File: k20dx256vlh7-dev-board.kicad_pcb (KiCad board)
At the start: 2 copper layers, 41 parts, among them J1 Conn_01x21_Male, J2 Conn_01x21_Male, J3 Conn_01x21_Male, J4 Conn_01x21_Male, J5 USB_C_Receptacle_USB2.0, J6 Conn_01x06_Male, SW1 Program, SW2 Reset, U1 MCP2562-E-SN, U2 MK20DX256VLH7, U3 NJM2884U1, U4 MKL04Z32VLC4, Y1 16MHz

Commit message: 回路図を更新
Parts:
- removed C3: 0.1u, Capacitor_SMD:C_0603_1608Metric
- removed C8: 2.2u, Capacitor_SMD:C_0805_2012Metric
- J1, J2, J3, J4, J6: moved to B.Cu
- moved SW2 116.0 mm to (223.5, 80.0), turned to 90 degrees
- moved J3 113.1 mm to (228.6, 127.0)
- moved J1 106.7 mm to (226.1, 127.0)
- moved J2 101.2 mm to (205.7, 127.0)
- moved J4 99.4 mm to (208.3, 127.0)
- moved C1 93.9 mm to (217.2, 116.6)
- moved R9 90.0 mm to (223.5, 86.9), turned to 270 degrees
- moved C9 86.7 mm to (223.5, 107.4), turned to 270 degrees
- moved J6 86.3 mm to (223.5, 76.2), turned to 90 degrees
- moved C4 85.2 mm to (222.0, 108.9), turned to 270 degrees
- moved R8 83.7 mm to (223.4, 123.6), turned to 90 degrees
- moved R1 81.8 mm to (220.9, 118.7), turned to 180 degrees
- moved C10 81.7 mm to (217.0, 118.4), turned to 180 degrees
- moved Y1 81.1 mm to (223.5, 91.4), turned to 90 degrees
- moved D2 78.3 mm to (220.0, 109.4)
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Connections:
- J1 pad 1: +5V -> GND
- J1 pad 15: Net-(J1-Pad15) -> /INTERNAL_LED
- J1 pad 16: /INTERNAL_LED -> Net-(J1-Pad16)
- J1 pad 2: +3V3 -> Net-(J1-Pad2)
- J1 pad 5: Net-(J1-Pad5) -> /CAN+
- J1 pad 6: /CAN+ -> /CAN-
- J1 pad 7: /CAN- -> Net-(J1-Pad7)
- J2 pad 1: GND -> +5V
- J2 pad 2: Net-(J2-Pad2) -> +3V3
- J3 pad 1: +5V -> GND
- J3 pad 15: Net-(J1-Pad15) -> /INTERNAL_LED
- J3 pad 16: /INTERNAL_LED -> Net-(J1-Pad16)
- J3 pad 2: +3V3 -> Net-(J1-Pad2)
- J3 pad 5: Net-(J1-Pad5) -> /CAN+
- J3 pad 6: /CAN+ -> /CAN-
- J3 pad 7: /CAN- -> Net-(J1-Pad7)
- J4 pad 1: GND -> +5V
- J4 pad 2: Net-(J2-Pad2) -> +3V3
- U2 pad 1: Net-(J2-Pad9) -> Net-(J2-Pad10)
- U2 pad 10: Net-(J2-Pad6) -> Net-(J2-Pad7)
- U2 pad 11: Net-(J2-Pad4) -> Net-(J2-Pad5)
- U2 pad 12: Net-(J2-Pad3) -> Net-(J2-Pad4)
- U2 pad 18: Net-(J2-Pad2) -> Net-(J2-Pad3)
- U2 pad 2: Net-(J2-Pad14) -> Net-(J2-Pad15)
- U2 pad 26: Net-(J2-Pad7) -> Net-(J2-Pad8)
- U2 pad 27: Net-(J2-Pad16) -> Net-(J2-Pad17)
- U2 pad 35: Net-(J1-Pad19) -> Net-(J1-Pad18)
- U2 pad 36: Net-(J1-Pad20) -> Net-(J1-Pad19)
- U2 pad 37: Net-(J2-Pad21) -> Net-(J1-Pad21)
- U2 pad 38: Net-(J1-Pad21) -> Net-(J1-Pad20)
- U2 pad 39: Net-(J1-Pad3) -> Net-(J1-Pad2)
- U2 pad 40: Net-(J1-Pad4) -> Net-(J1-Pad3)
- U2 pad 41: Net-(J2-Pad8) -> Net-(J2-Pad9)
- U2 pad 42: Net-(J2-Pad15) -> Net-(J2-Pad16)
- U2 pad 43: Net-(J1-Pad18) -> Net-(J1-Pad17)
- U2 pad 44: Net-(J2-Pad18) -> Net-(J2-Pad19)
- U2 pad 45: Net-(J2-Pad17) -> Net-(J2-Pad18)
- U2 pad 46: Net-(J1-Pad12) -> Net-(J1-Pad11)
- U2 pad 49: Net-(J1-Pad13) -> Net-(J1-Pad12)
- U2 pad 51: Net-(J1-Pad14) -> Net-(J1-Pad13)
- U2 pad 52: Net-(J1-Pad15) -> Net-(J1-Pad14)
- U2 pad 53: Net-(J2-Pad12) -> Net-(J2-Pad13)
- U2 pad 54: Net-(J2-Pad13) -> Net-(J2-Pad14)
- U2 pad 55: Net-(J2-Pad11) -> Net-(J2-Pad12)
- U2 pad 56: Net-(J2-Pad10) -> Net-(J2-Pad11)
- U2 pad 57: Net-(J1-Pad5) -> Net-(J1-Pad4)
- U2 pad 58: Net-(J1-Pad17) -> Net-(J1-Pad16)
- U2 pad 59: Net-(J1-Pad10) -> Net-(J1-Pad9)
- U2 pad 60: Net-(J1-Pad11) -> Net-(J1-Pad10)
- U2 pad 61: Net-(J1-Pad9) -> Net-(J1-Pad8)
- U2 pad 62: Net-(J2-Pad20) -> Net-(J2-Pad21)
- U2 pad 63: Net-(J2-Pad19) -> Net-(J2-Pad20)
- U2 pad 64: Net-(J1-Pad8) -> Net-(J1-Pad7)
- U2 pad 9: Net-(J2-Pad5) -> Net-(J2-Pad6)
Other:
- board outline added: 25.4 x 53.3 mm
- net class 0.2 added: clearance 0.1778, trace_width 0.2, via_dia 0.8, via_drill 0.4
- net class 0.25 added: clearance 0.1778, trace_width 0.25, via_dia 0.8, via_drill 0.4
- net class 0.5 added: clearance 0.1778, trace_width 0.5, via_dia 0.8, via_drill 0.4

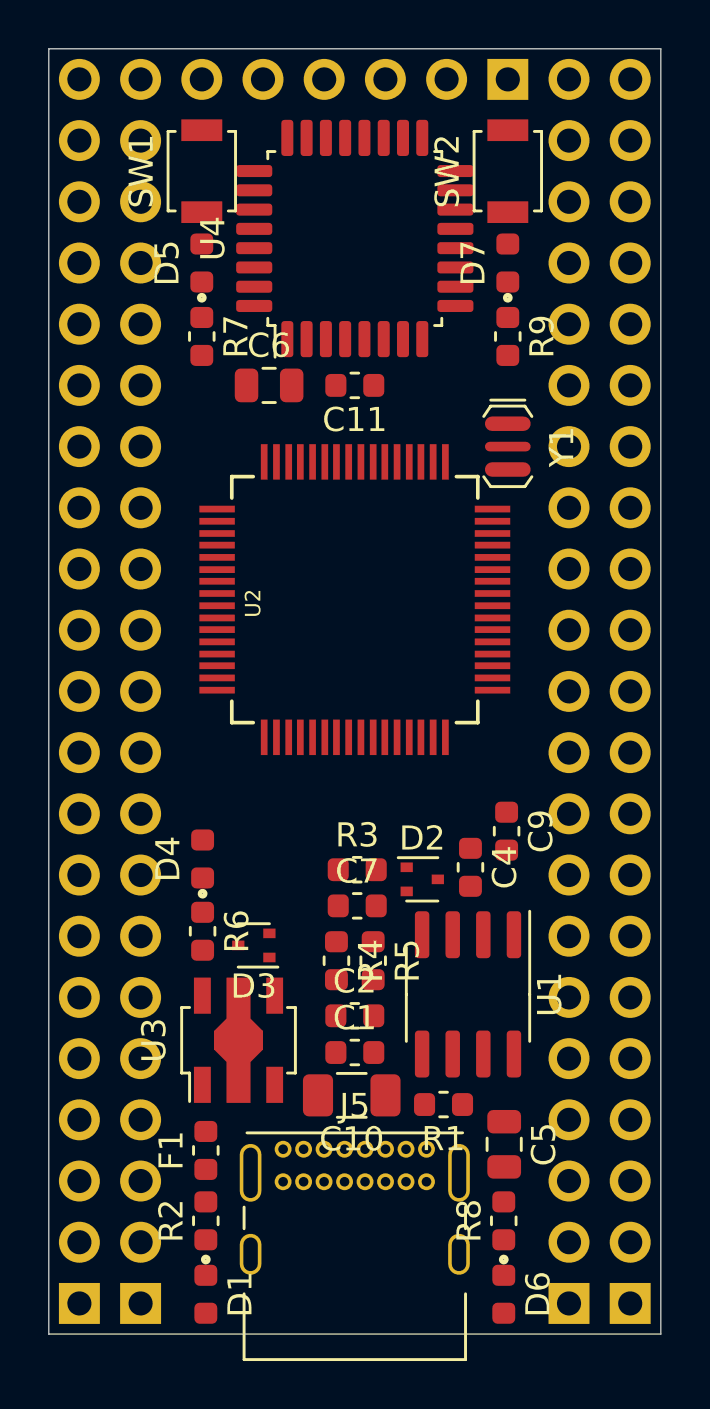
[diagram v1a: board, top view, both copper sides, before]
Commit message: フットプリントの変更
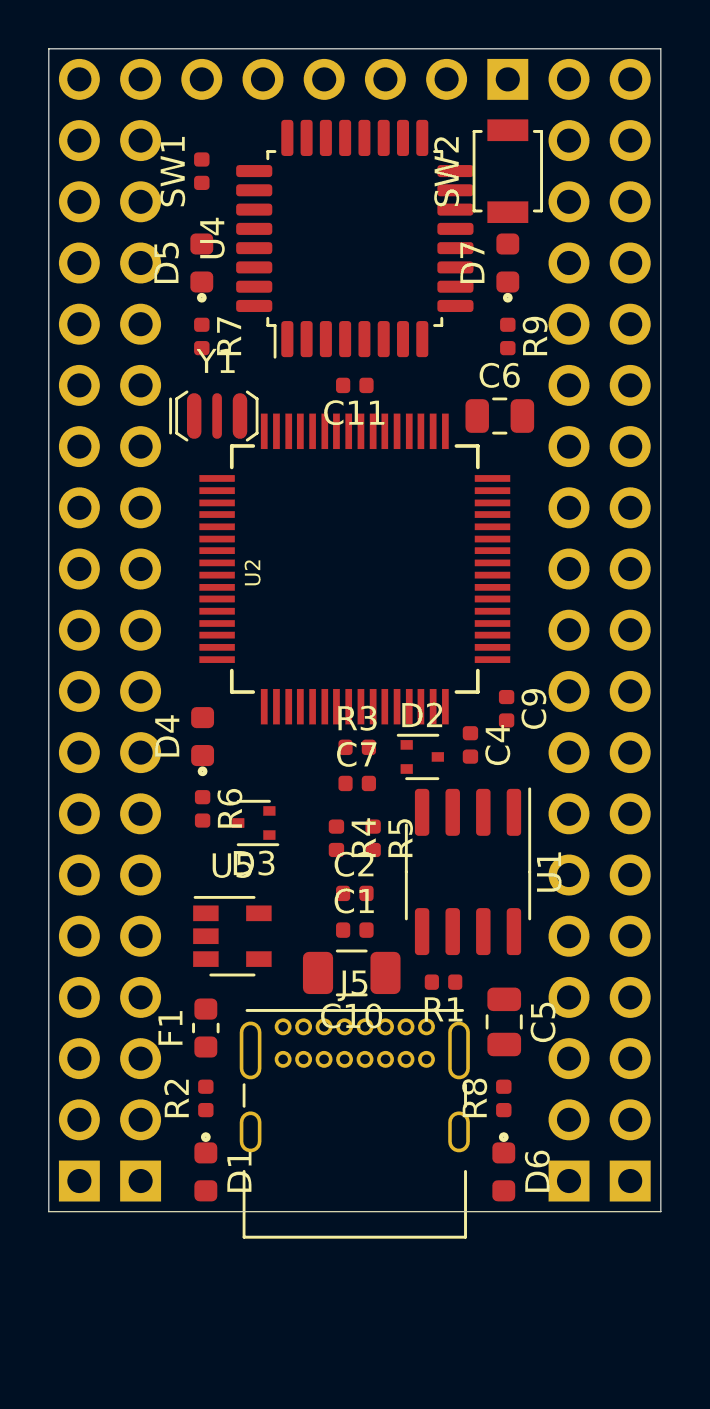
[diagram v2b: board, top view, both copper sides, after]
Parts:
- removed U3: NJM2884U1, Package_TO_SOT_SMD:SOT-89-5
- added U5: MIC5219-3.3YM5, Package_TO_SOT_SMD:SOT-23-5, F.Cu at (212.1, 111.8)
- C1, C11, C2, C4, C7, C9: value 0.1u -> 0.1u, 50v; footprint Capacitor_SMD:C_0603_1608Metric -> Capacitor_SMD:C_0402_1005Metric
- J1, J2, J3, J4: value Conn_01x21_Male -> Conn_01x19_Male; footprint Connector_PinHeader_2.54mm:PinHeader_1x21_P2.54mm_Vertical -> Connector_PinHeader_2.54mm:PinHeader_1x19_P2.54mm_Vertical
- R1, R2, R3, R4, R5, R6, R7, R8, R9: footprint Resistor_SMD:R_0603_1608Metric -> Resistor_SMD:R_0402_1005Metric
- SW1: footprint Button_Switch_SMD:SW_SPST_B3U-1000P -> Capacitor_SMD:C_0402_1005Metric
- moved Y1 12.1 mm to (211.5, 90.2), turned to 180 degrees
- moved C6 9.66 mm to (223.2, 90.2)
- moved J1 5.68 mm to (228.6, 121.9)
- moved J3 5.68 mm to (226.1, 121.9)
- moved C4 5.08 mm to (222.0, 103.8)
- moved C9 5.08 mm to (223.5, 102.3)
- moved D2 5.08 mm to (220.0, 104.3)
- moved F1 5.08 mm to (211.0, 115.6)
- moved C1 5.08 mm to (217.2, 111.5)
- moved C10 5.08 mm to (217.0, 113.3)
- moved C2 5.08 mm to (217.2, 110.0)
- moved C5 5.08 mm to (223.4, 115.3)
- moved C7 5.08 mm to (217.3, 105.4)
- moved D1 5.08 mm to (211.0, 121.5)
- moved D3 5.08 mm to (213.0, 107.1)
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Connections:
- U2 pad 1: Net-(J2-Pad10) -> Net-(J2-Pad6)
- U2 pad 10: Net-(J2-Pad7) -> Net-(U2-Pad10)
- U2 pad 11: Net-(J2-Pad5) -> Net-(U2-Pad11)
- U2 pad 12: Net-(J2-Pad4) -> Net-(U2-Pad12)
- U2 pad 2: Net-(J2-Pad15) -> Net-(J2-Pad11)
- U2 pad 26: Net-(J2-Pad8) -> Net-(J2-Pad4)
- U2 pad 27: Net-(J2-Pad17) -> Net-(J2-Pad13)
- U2 pad 37: Net-(J1-Pad21) -> Net-(J2-Pad18)
- U2 pad 38: Net-(J1-Pad20) -> Net-(J2-Pad19)
- U2 pad 41: Net-(J2-Pad9) -> Net-(J2-Pad5)
- U2 pad 42: Net-(J2-Pad16) -> Net-(J2-Pad12)
- U2 pad 44: Net-(J2-Pad19) -> Net-(J2-Pad15)
- U2 pad 45: Net-(J2-Pad18) -> Net-(J2-Pad14)
- U2 pad 53: Net-(J2-Pad13) -> Net-(J2-Pad9)
- U2 pad 54: Net-(J2-Pad14) -> Net-(J2-Pad10)
- U2 pad 55: Net-(J2-Pad12) -> Net-(J2-Pad8)
- U2 pad 56: Net-(J2-Pad11) -> Net-(J2-Pad7)
- U2 pad 62: Net-(J2-Pad21) -> Net-(J2-Pad17)
- U2 pad 63: Net-(J2-Pad20) -> Net-(J2-Pad16)
- U2 pad 9: Net-(J2-Pad6) -> Net-(U2-Pad9)
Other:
- board size 25.4 x 53.3 mm -> 25.4 x 48.3 mm

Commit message: 回路図の見直し
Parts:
- removed J4: Conn_01x19_Male, Connector_PinHeader_2.54mm:PinHeader_1x19_P2.54mm_Vertical
- removed J6: Conn_01x06_Male, Connector_PinHeader_2.54mm:PinHeader_1x06_P2.54mm_Vertical
- J3: value Conn_01x19_Male -> Conn_01x08_Male; footprint Connector_PinHeader_2.54mm:PinHeader_1x19_P2.54mm_Vertical -> Connector_PinHeader_2.54mm:PinHeader_1x08_P2.54mm_Vertical
- SW1: footprint Capacitor_SMD:C_0402_1005Metric -> Button_Switch_SMD:SW_SPST_B3U-1000P
- moved J3 45.7 mm to (226.1, 76.2), turned to 90 degrees
- moved D3 13.6 mm to (208.5, 119.9), turned to 270 degrees
- moved Y1 12.0 mm to (223.4, 90.3), turned to 135 degrees
- moved R6 9.57 mm to (208.9, 97.1)
- moved D4 9.33 mm to (208.9, 94.3)
- moved D2 8.98 mm to (225.9, 97.6), turned to 270 degrees
- moved C10 8.52 mm to (209.6, 117.3), turned to 0 degrees
- moved R1 7.04 mm to (226.3, 109.2), turned to 270 degrees
- moved C1 6.73 mm to (223.8, 112.8)
- moved R9 6.30 mm to (222.9, 80.6)
- moved R7 6.30 mm to (211.4, 80.6)
- moved F1 6.12 mm to (216.7, 113.3), turned to 0 degrees
- moved C4 5.54 mm to (224.4, 98.8)
- moved D7 5.39 mm to (222.2, 78.6), turned to 180 degrees
- moved D5 5.39 mm to (212.2, 78.6), turned to 0 degrees
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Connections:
- J3 pad 1: GND -> /RESET
- J3 pad 2: Net-(J1-Pad2) -> /PTA0
- J3 pad 3: Net-(J1-Pad3) -> /PTA1
- J3 pad 4: Net-(J1-Pad4) -> /PTA2
- J3 pad 5: /CAN+ -> /PTA3
- J3 pad 6: /CAN- -> /Program
- J3 pad 7: Net-(J1-Pad7) -> +3V3
- J3 pad 8: Net-(J1-Pad8) -> GND
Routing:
- net +3V3: track 0.00 -> 38.1 mm, vias 0 -> 1
- net GND: track 0.00 -> 32.9 mm
- net +5V: track 0.00 -> 25.3 mm
- net /USB_D+: track 0.00 -> 13.0 mm, vias 0 -> 1
- net /USB_D-: track 0.00 -> 13.0 mm, vias 0 -> 1
- net Net-(C5-Pad1): track 0.00 -> 12.1 mm
- net /CAN+: track 0.00 -> 11.4 mm
- net /CAN-: track 0.00 -> 4.65 mm
- net Net-(C4-Pad1): track 0.00 -> 3.09 mm
- net Net-(D1-Pad1): track 0.00 -> 2.95 mm
- net Net-(U2-Pad32): track 0.00 -> 2.32 mm
- net Net-(U2-Pad33): track 0.00 -> 2.32 mm
- net /USB_P: track 0.00 -> 1.65 mm
- net /USB_M: track 0.00 -> 1.65 mm

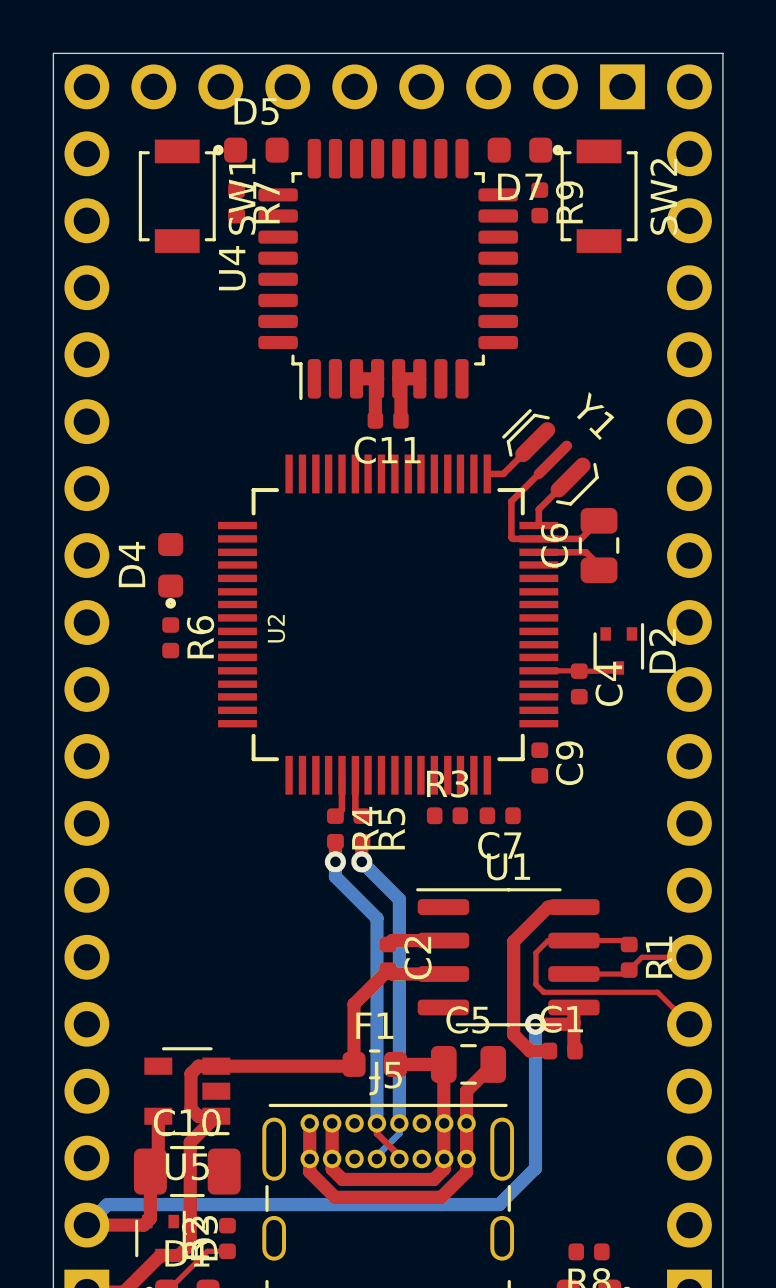
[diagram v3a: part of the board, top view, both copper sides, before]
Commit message: 回路図に追記
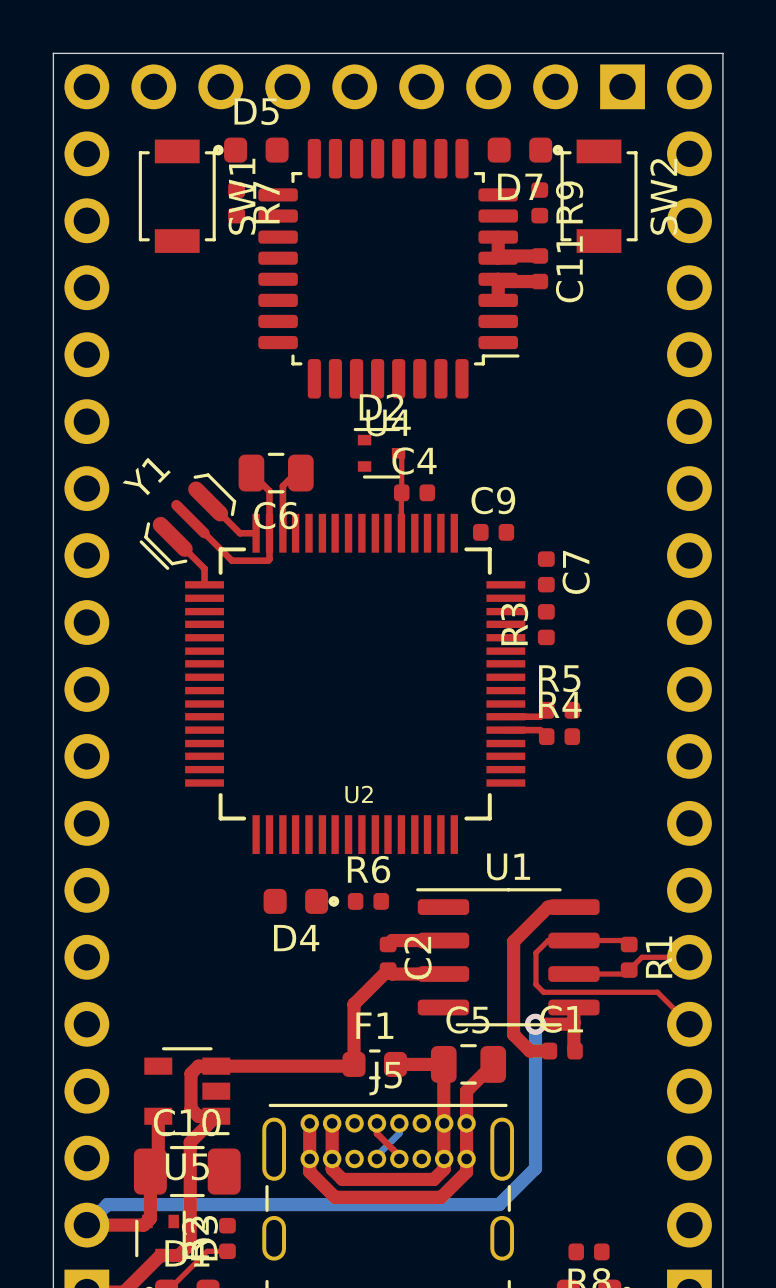
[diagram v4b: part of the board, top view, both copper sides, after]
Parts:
- moved Y1 13.9 mm to (209.7, 92.6), turned to 225 degrees
- moved D4 13.6 mm to (213.7, 107.1), turned to 180 degrees
- moved C6 12.6 mm to (212.9, 90.8), turned to 180 degrees
- moved R6 12.5 mm to (216.4, 107.1), turned to 0 degrees
- moved D2 11.7 mm to (216.9, 90.1), turned to 0 degrees
- moved C4 9.57 mm to (218.2, 91.6), turned to 0 degrees
- moved C7 9.41 mm to (223.2, 94.6), turned to 270 degrees
- moved R4 9.19 mm to (223.7, 100.8), turned to 0 degrees
- moved C9 8.92 mm to (221.2, 93.1), turned to 0 degrees
- moved R5 8.75 mm to (223.7, 99.8), turned to 0 degrees
- moved R3 8.16 mm to (223.2, 96.6), turned to 90 degrees
- moved C11 8.13 mm to (222.9, 83.1), turned to 270 degrees
- moved U2 2.57 mm to (215.9, 98.8), turned to 180 degrees
- turned U4 to 180 degrees
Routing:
- net /USB_D+: track 13.0 -> 1.70 mm, vias 1 -> 0
- net /USB_D-: track 13.0 -> 1.70 mm, vias 1 -> 0

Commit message: 発注した！
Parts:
- added J4: Conn_01x05_Male, Connector_PinHeader_2.54mm:PinHeader_1x05_P2.54mm_Vertical, B.Cu at (231.1, 109.2)
- added J6: Conn_01x12_Male, Connector_PinHeader_2.54mm:PinHeader_1x12_P2.54mm_Vertical, B.Cu at (264.2, 119.4)
- J1: value Conn_01x19_Male -> Conn_01x12_Male; footprint Connector_PinHeader_2.54mm:PinHeader_1x19_P2.54mm_Vertical -> Connector_PinHeader_2.54mm:PinHeader_1x12_P2.54mm_Vertical
- J2: value Conn_01x19_Male -> Conn_01x13_Male; footprint Connector_PinHeader_2.54mm:PinHeader_1x19_P2.54mm_Vertical -> Connector_PinHeader_2.54mm:PinHeader_1x13_P2.54mm_Vertical
- moved J2 63.7 mm to (261.6, 91.4), turned to 90 degrees
- moved SW1 62.5 mm to (261.1, 115.1), turned to 90 degrees
- moved D5 59.8 mm to (258.1, 116.9), turned to 180 degrees
- moved R7 58.5 mm to (258.9, 114.9), turned to 90 degrees
- moved J3 55.9 mm to (261.6, 119.4)
- moved C11 46.7 mm to (255.5, 116.6), turned to 225 degrees
- moved U4 45.2 mm to (251.4, 112.5), turned to 135 degrees
- moved Y1 45.1 mm to (254.2, 100.0), turned to 90 degrees
- moved C6 42.1 mm to (253.1, 103.5), turned to 45 degrees
- moved C2 38.7 mm to (255.5, 103.3), turned to 225 degrees
- moved D7 38.6 mm to (257.6, 94.0)
- moved R9 38.6 mm to (258.4, 96.0)
- moved SW2 38.6 mm to (260.6, 95.7)
- moved D3 37.3 mm to (244.5, 110.0), turned to 90 degrees
- moved D2 37.2 mm to (250.8, 105.5), turned to 225 degrees
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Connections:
- net Net-(J1-Pad9) renamed /D7(59)
- J1 pad 10: Net-(J1-Pad10) -> /D14(58)
- J1 pad 11: Net-(J1-Pad11) -> /D2(57)
- J1 pad 12: Net-(J1-Pad12) -> /D30(56)
- J1 pad 2: Net-(J1-Pad2) -> /D26(2)
- J1 pad 3: Net-(J1-Pad3) -> /D31(1)
- J1 pad 4: Net-(J1-Pad4) -> /D5(64)
- J1 pad 5: /CAN+ -> /D21(63)
- J1 pad 6: /CAN- -> /D20(62)
- J1 pad 7: Net-(J1-Pad7) -> /D6(61)
- J1 pad 8: Net-(J1-Pad8) -> /D8(60)
- J2 pad 1: +5V -> /D32(41)
- J2 pad 10: Net-(J2-Pad10) -> /D12(52)
- J2 pad 11: Net-(J2-Pad11) -> /D28(53)
- J2 pad 12: Net-(J2-Pad12) -> /D27(54)
- J2 pad 13: Net-(J2-Pad13) -> /D29(55)
- J2 pad 2: +3V3 -> /D25(42)
- J2 pad 3: Net-(J2-Pad3) -> /D15(43)
- J2 pad 4: Net-(J2-Pad4) -> /D22(44)
- J2 pad 5: Net-(J2-Pad5) -> /D23(45)
- J2 pad 6: Net-(J2-Pad6) -> /D9(46)
- J2 pad 7: Net-(J2-Pad7) -> /D10(49)
- J2 pad 8: Net-(J2-Pad8) -> /D13(50)_LED
- J2 pad 9: Net-(J2-Pad9) -> /D11(51)
- U2 pad 1: Net-(J2-Pad6) -> /D31(1)
- U2 pad 18: Net-(J2-Pad3) -> Net-(J4-Pad5)
- U2 pad 2: Net-(J2-Pad11) -> /D26(2)
- U2 pad 26: Net-(J2-Pad4) -> /D33(26)
- U2 pad 27: Net-(J2-Pad13) -> /D24(27)
- U2 pad 35: Net-(J1-Pad18) -> /D16(35)
- U2 pad 36: Net-(J1-Pad19) -> /D17(36)
- U2 pad 37: Net-(J2-Pad18) -> /D19(37)
- U2 pad 38: Net-(J2-Pad19) -> /D18(38)
- U2 pad 39: Net-(J1-Pad2) -> /D0(39)
- U2 pad 40: Net-(J1-Pad3) -> /D1(40)
- U2 pad 41: Net-(J2-Pad5) -> /D32(41)
- U2 pad 42: Net-(J2-Pad12) -> /D25(42)
- U2 pad 43: Net-(J1-Pad17) -> /D15(43)
- U2 pad 44: Net-(J2-Pad15) -> /D22(44)
- U2 pad 45: Net-(J2-Pad14) -> /D23(45)
- U2 pad 46: Net-(J1-Pad11) -> /D9(46)
- U2 pad 49: Net-(J1-Pad12) -> /D10(49)
- U2 pad 50: /INTERNAL_LED -> /D13(50)_LED
- U2 pad 51: Net-(J1-Pad13) -> /D11(51)
- U2 pad 52: Net-(J1-Pad14) -> /D12(52)
- U2 pad 53: Net-(J2-Pad9) -> /D28(53)
- U2 pad 54: Net-(J2-Pad10) -> /D27(54)
- U2 pad 55: Net-(J2-Pad8) -> /D29(55)
- U2 pad 56: Net-(J2-Pad7) -> /D30(56)
- U2 pad 57: Net-(J1-Pad4) -> /D2(57)
- U2 pad 58: Net-(J1-Pad16) -> /D14(58)
- U2 pad 60: Net-(J1-Pad10) -> /D8(60)
- U2 pad 61: Net-(J1-Pad8) -> /D6(61)
- U2 pad 62: Net-(J2-Pad17) -> /D20(62)
- U2 pad 63: Net-(J2-Pad16) -> /D21(63)
- U2 pad 64: Net-(J1-Pad7) -> /D5(64)
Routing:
- net GND: track 32.9 -> 144.7 mm, vias 0 -> 3
- net +3V3: track 38.1 -> 134.7 mm, vias 1 -> 4
- net /RESET: track 0.00 -> 49.0 mm, vias 0 -> 3
- net /Program: track 0.00 -> 28.6 mm, vias 0 -> 1
- net /PTA1: track 0.00 -> 26.9 mm, vias 0 -> 2
- net /PTA0: track 0.00 -> 26.0 mm, vias 0 -> 2
- net +5V: track 25.3 -> 48.7 mm, vias 0 -> 2
- net /PTA3: track 0.00 -> 21.6 mm, vias 0 -> 3
- net /D33(26): track 0.00 -> 21.6 mm, vias 0 -> 1
- net /D26(2): track 0.00 -> 19.5 mm, vias 0 -> 1
- net /D24(27): track 0.00 -> 18.7 mm, vias 0 -> 1
- net /D5(64): track 0.00 -> 18.6 mm
- net /D31(1): track 0.00 -> 18.3 mm, vias 0 -> 1
- net /PTA2: track 0.00 -> 17.7 mm, vias 0 -> 1
- net /D2(57): track 0.00 -> 17.6 mm, vias 0 -> 1
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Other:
- board size 25.4 x 48.3 mm -> 35.8 x 28.2 mm
- board text added: "k20-dev @NJL7502L"
